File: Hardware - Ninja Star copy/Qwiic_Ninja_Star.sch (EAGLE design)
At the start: 21 parts, among them J1 QWIIC_RIGHT_ANGLE, J2 QWIIC_RIGHT_ANGLE, J3 QWIIC_RIGHT_ANGLE, J4 QWIIC_RIGHT_ANGLE, J5 QWIIC_RIGHT_ANGLE

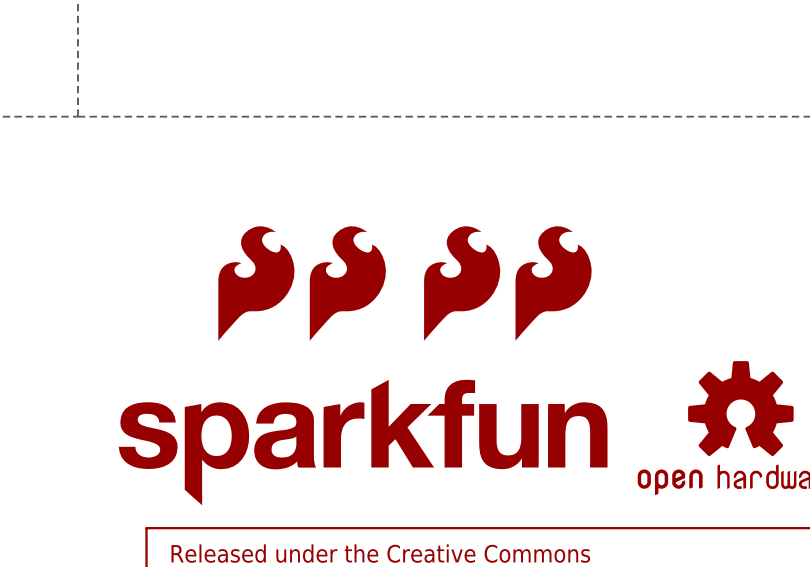
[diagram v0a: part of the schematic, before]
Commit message: Wired qwiic ninja star
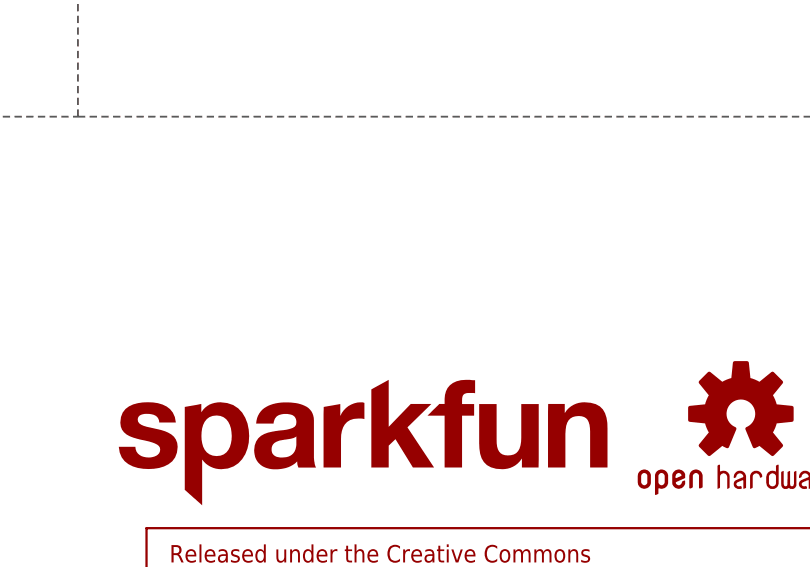
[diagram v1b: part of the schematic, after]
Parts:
- removed LOGO5, LOGO6, LOGO7, LOGO8: SFE_LOGO_FLAME.1_INCH, SparkFun-Aesthetics:SFE_LOGO_FLAME.1_INCH
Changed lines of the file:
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@@
 <part name="LOGO3" library="SparkFun-Aesthetics" deviceset="OSHW-LOGO" device="S"/>
 <part name="LOGO4" library="SparkFun-Aesthetics" deviceset="SFE_LOGO_NAME" device=".2_INCH"/>
-<part name="LOGO5" library="SparkFun-Aesthetics" deviceset="SFE_LOGO_FLAME" device=".1_INCH"/>
-<part name="LOGO6" library="SparkFun-Aesthetics" deviceset="SFE_LOGO_FLAME" device=".1_INCH"/>
-<part name="LOGO7" library="SparkFun-Aesthetics" deviceset="SFE_LOGO_FLAME" device=".1_INCH"/>
-<part name="LOGO8" library="SparkFun-Aesthetics" deviceset="SFE_LOGO_FLAME" device=".1_INCH"/>
 <part name="J5" library="SparkFun-Connectors" deviceset="QWIIC_CONNECTOR" device="JS-1MM" value="QWIIC_RIGHT_ANGLE"/>
 <part name="GND6" library="SparkFun-PowerSymbols" deviceset="GND" device=""/>
@@
 <instance part="LOGO3" gate="G$1" x="213.36" y="48.26" smashed="yes"/>
 <instance part="LOGO4" gate="G$1" x="142.24" y="38.1" smashed="yes"/>
-<instance part="LOGO5" gate="G$1" x="154.94" y="55.88" smashed="yes"/>
-<instance part="LOGO6" gate="G$1" x="165.1" y="55.88" smashed="yes"/>
-<instance part="LOGO7" gate="G$1" x="177.8" y="55.88" smashed="yes"/>
-<instance part="LOGO8" gate="G$1" x="187.96" y="55.88" smashed="yes"/>
 <instance part="J5" gate="G$1" x="55.88" y="40.64" smashed="yes">
 <attribute name="VALUE" x="50.8" y="27.686" size="1.778" layer="96" font="vector" align="top-left"/>
